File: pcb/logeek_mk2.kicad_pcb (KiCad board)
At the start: 2 copper layers, 68.6 x 53.3 mm, 138 parts, among them P1 Power, P10 XH2.54-2P RA, P11 BARREL_JACK, P12 USB_B, P13 DC3 5x2, P14 Power, P15 Analog, P16 Digital, P17 Digital, P2 Analog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

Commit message: Part value update.
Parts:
- C18: value 22uF -> 10uF
- D1, D2, D3, D7: value 1N5819 -> 1N5819WS
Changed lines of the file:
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@@
     (visible_elements 7FFDF121)
     (pcbplotparams
-      (layerselection 0x00020_00000000)
+      (layerselection 0x010fc_80000001)
       (usegerberextensions false)
       (excludeedgelayer false)
       (linewidth 0.100000)
-      (plotframeref false)
+      (plotframeref true)
       (viasonmask false)
       (mode 1)
@@
       (psa4output false)
       (plotreference true)
-      (plotvalue true)
-      (plotinvisibletext true)
+      (plotvalue false)
+      (plotinvisibletext false)
       (padsonsilk false)
       (subtractmaskfromsilk false)
       (outputformat 4)
       (mirror false)
-      (drillshape 0)
+      (drillshape 2)
       (scaleselection 1)
       (outputdirectory gerber/))
@@
       (effects (font (size 0.8 0.8) (thickness 0.15)))
     )
-    (fp_text value 1N5819 (at 0 0 270) (layer F.Fab)
+    (fp_text value 1N5819WS (at 0 0 270) (layer F.Fab)
       (effects (font (size 0.8 0.8) (thickness 0.15)))
     )
@@
       (effects (font (size 0.8 0.8) (thickness 0.15)))
     )
-    (fp_text value 22uF (at 0 0 270) (layer F.Fab)
+    (fp_text value 10uF (at 0 0 270) (layer F.Fab)
       (effects (font (size 0.8 0.8) (thickness 0.15)))
     )
@@
       (effects (font (size 0.8 0.8) (thickness 0.15)))
     )
-    (fp_text value 1N5819 (at 0 0 270) (layer F.Fab)
+    (fp_text value 1N5819WS (at 0 0 270) (layer F.Fab)
       (effects (font (size 0.8 0.8) (thickness 0.15)))
     )
@@
       (effects (font (size 0.8 0.8) (thickness 0.15)))
     )
-    (fp_text value 1N5819 (at -0.635 0) (layer F.Fab)
+    (fp_text value 1N5819WS (at -0.635 0) (layer F.Fab)
       (effects (font (size 0.8 0.8) (thickness 0.15)))
     )
@@
       (effects (font (size 1 1) (thickness 0.15)))
     )
-    (fp_text value 1N5819 (at -0.635 0) (layer F.Fab)
+    (fp_text value 1N5819WS (at -0.635 0) (layer F.Fab)
       (effects (font (size 0.8 0.8) (thickness 0.15)))
     )

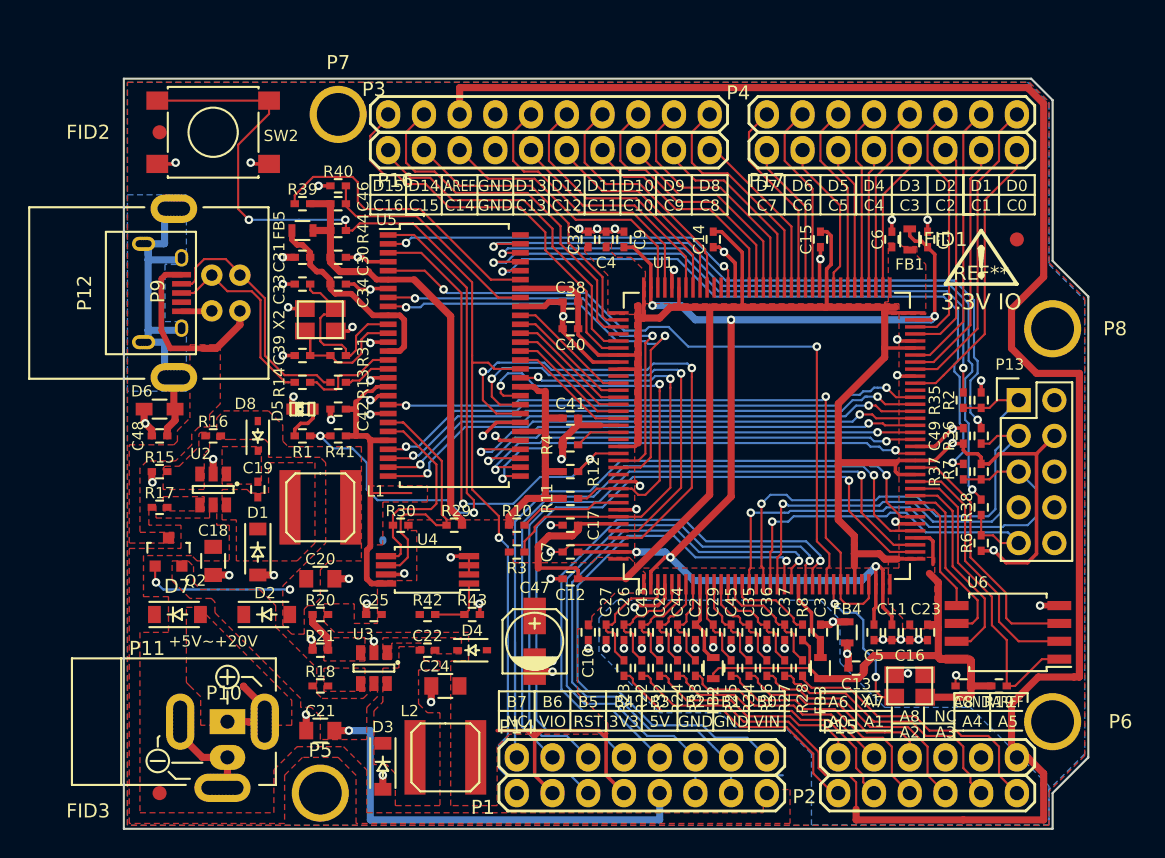
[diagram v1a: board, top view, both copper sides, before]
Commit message: Corrected FPGA footprint. Delete extra oscillator. Update silkscreen.
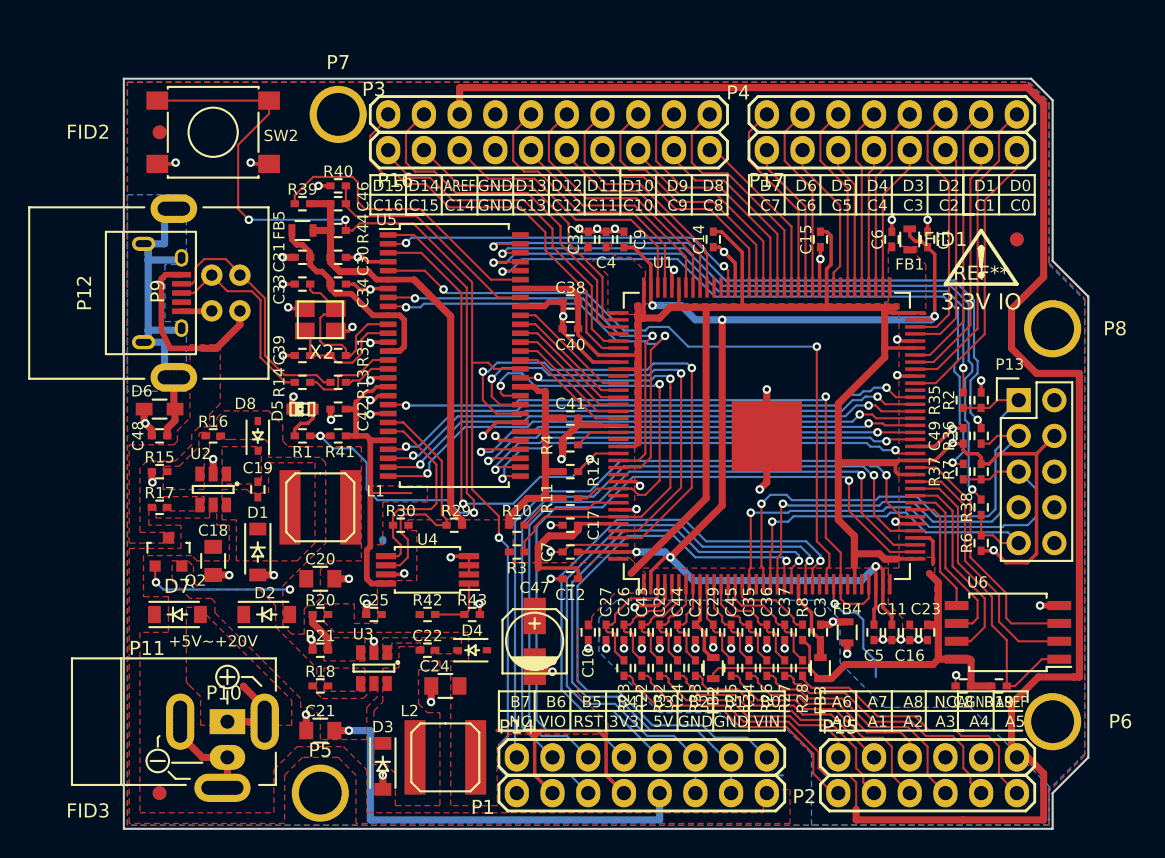
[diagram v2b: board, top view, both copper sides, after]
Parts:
- removed C13: 0.1uF, Capacitors_SMD:C_0402
- removed X1: 25MHz 50ppm, OSC3225
- C27, C28, C29, C35, C36, C37, C43, C44, C45: value 0.1uF -> 1nF
- R1, R41: value 220 -> 330
- U1: footprint Housings_QFP:TQFP-144_20x20mm_Pitch0.5mm -> Logeek_MK2:TQFP-144EP_20x20mm_Pitch0.5mm
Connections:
- U1 pad 28: /USERCLK -> Net-(U1-Pad28)
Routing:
- net +3V3: track 297.6 -> 286.0 mm
- net /USERCLK: track 10.9 -> 0.00 mm, vias 2 -> 0
- net Net-(U1-Pad28): track 0.00 -> 8.36 mm, vias 0 -> 1
- net GNDD: track 126.9 -> 132.2 mm, vias 63 -> 64

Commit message: Updated socket footprints.
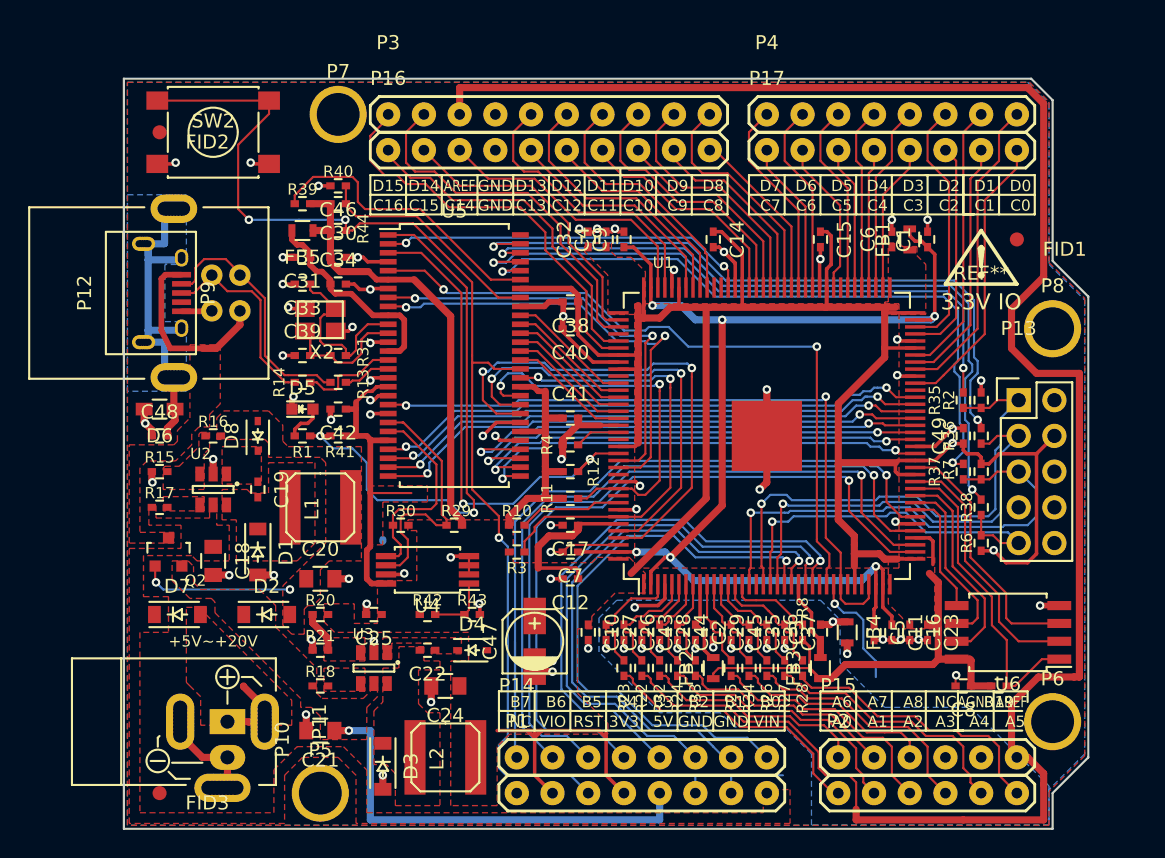
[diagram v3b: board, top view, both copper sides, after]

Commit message: Footprints update.
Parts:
- C47: footprint Capacitors_SMD:c_elec_4x5.8 -> Logeek_MK2:TantalC_SizeB_EIA-3528_HandSoldering
- D5: value LED GREEN -> LED TRUE GREEN; footprint LEDs:LED-0603 -> Logeek_MK2:LED-0603
- D6: footprint Resistors_SMD:R_0603_HandSoldering -> Logeek_MK2:R_0402_HandSoldering
- R41: value 330 -> 1K
- X2: footprint Crystals_Oscillators_SMD:crystal_FA238-TSX3225 -> Logeek_MK2:XTAL3225
- moved C47 0.64 mm to (140.2, 112.4)
- moved C8 0.13 mm to (170.7, 116.1)
- moved R19 0.13 mm to (173.2, 116.1)
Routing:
- net Net-(U1-Pad28): track 8.36 -> 0.00 mm, vias 1 -> 0
- net GNDD: track 132.2 -> 135.0 mm
- net +3V3: track 286.0 -> 287.7 mm, vias 2 -> 4

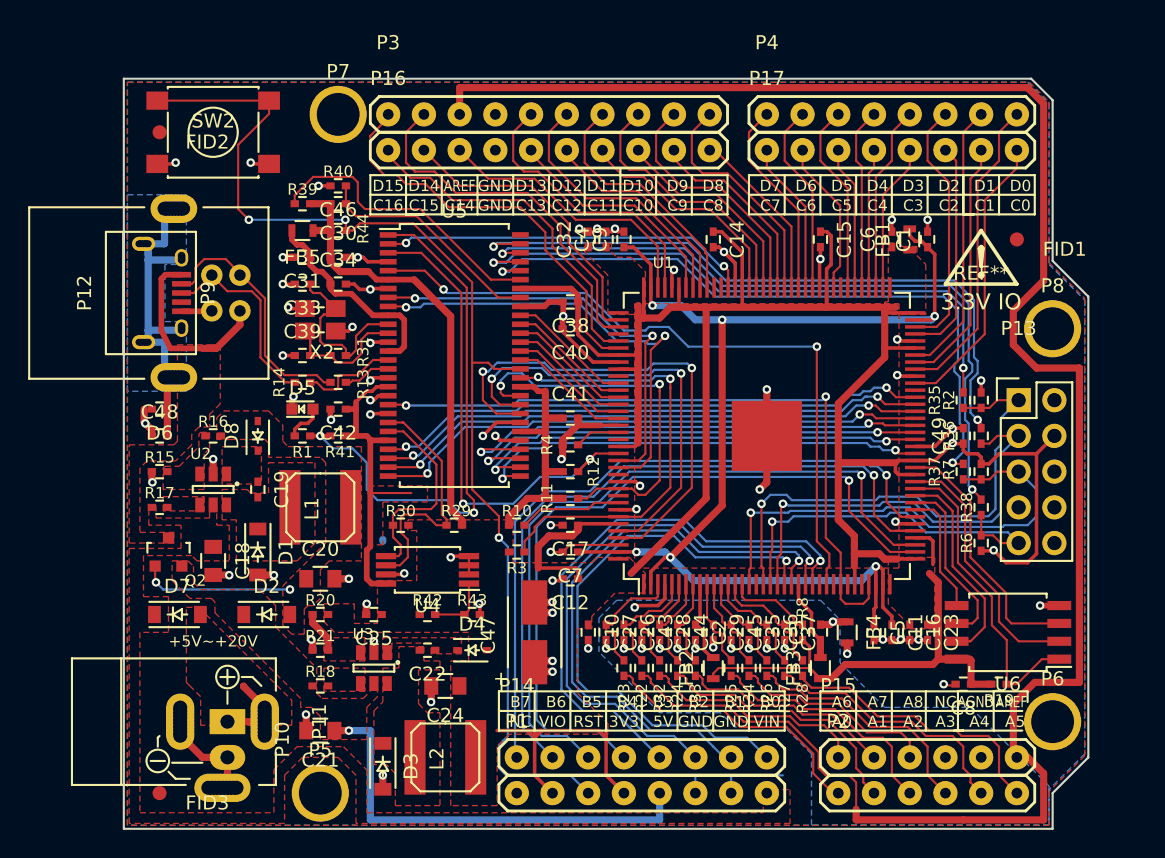
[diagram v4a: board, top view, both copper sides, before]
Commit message: Add EXTCLK.
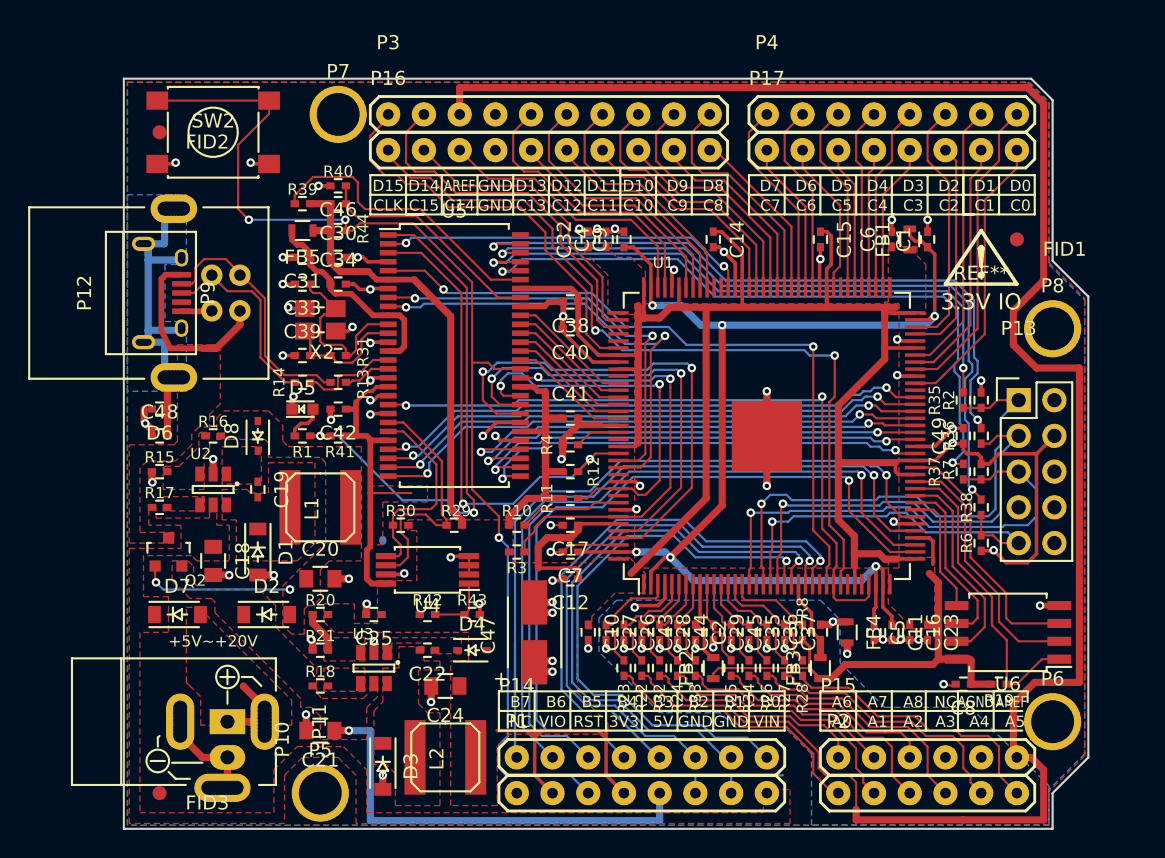
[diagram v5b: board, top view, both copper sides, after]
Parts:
- R41: value 1K -> 1k
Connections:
- P16 pad 1: /C16 -> /EXTCLK
- U1 pad 113: /C16 -> Net-(U1-Pad113)
- U1 pad 28: Net-(U1-Pad28) -> /IFCLK
- U1 pad 29: /IFCLK -> /EXTCLK
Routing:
- net /EXTCLK: track 0.00 -> 57.4 mm, vias 0 -> 2
- net /C16: track 24.7 -> 0.00 mm
- net /LEDEN: track 39.8 -> 38.7 mm
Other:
- board text added: "CLK"
- board text removed: "C16"

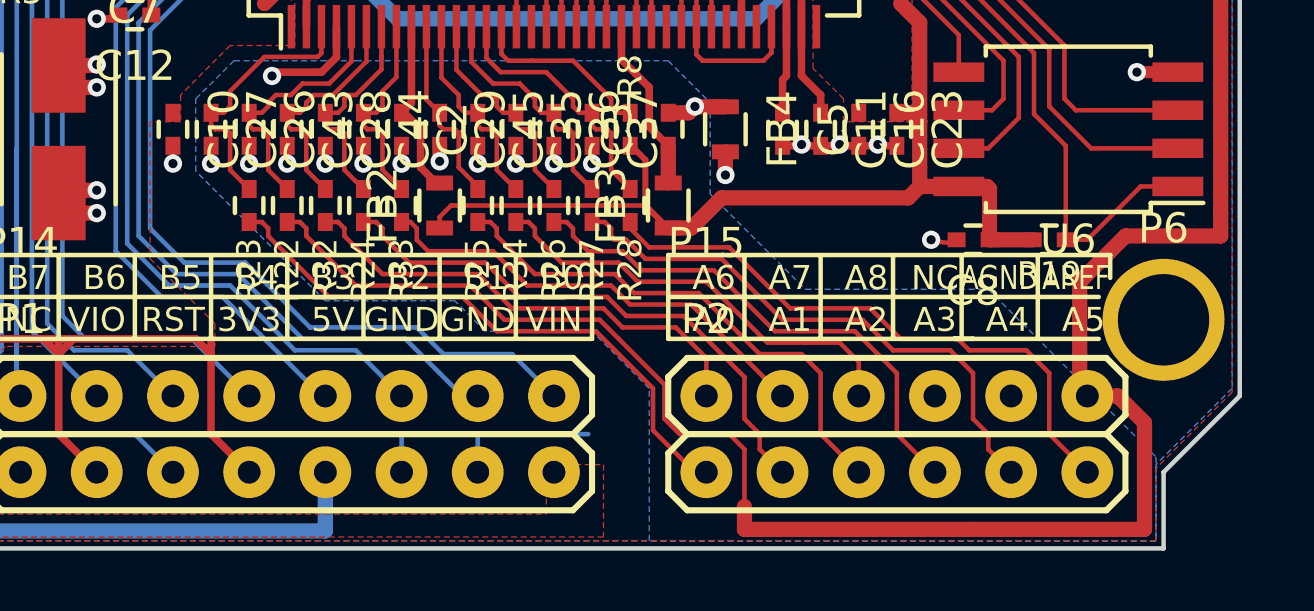
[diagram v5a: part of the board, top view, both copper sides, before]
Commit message: Analog pin-mapping changed to support VIN monitoring.
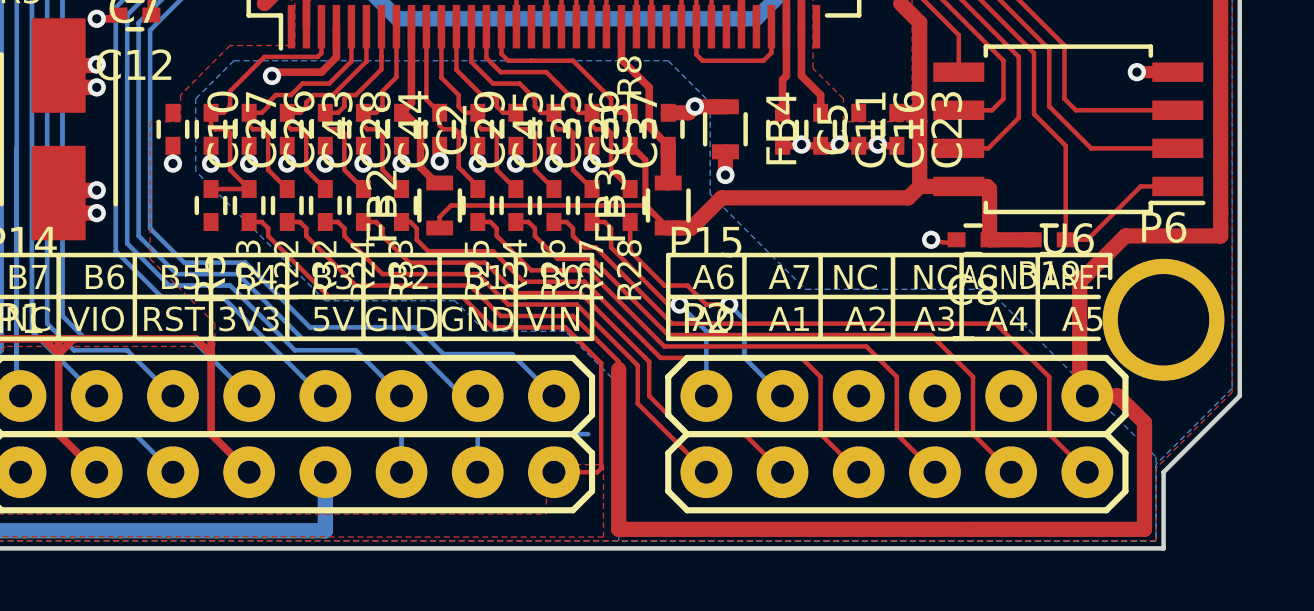
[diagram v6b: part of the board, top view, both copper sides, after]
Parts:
- added R5: 1k, Logeek_MK2:R_0402_HandSoldering, F.Cu at (145.3, 114.9)
- R23: value 22 -> 10k
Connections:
- C27 pad 1: /AIN0 -> /VMON
- C29 pad 1: /AIN2 -> /AIN3
- C35 pad 1: /AIN3 -> /AIN5
- C36 pad 1: /AIN4 -> /AIN6
- C37 pad 1: /AIN5 -> /AIN7
- C43 pad 1: /AIN6 -> /AIN0
- C44 pad 1: /AIN7 -> /AIN2
- C45 pad 1: /AIN8 -> /AIN4
- R23 pad 1: /AIN0 -> /VMON
- R23 pad 2: /A0 -> /VIN_SAFE
- R25 pad 1: /AIN2 -> /AIN3
- R25 pad 2: /A2 -> /A3
- R26 pad 1: /AIN3 -> /AIN5
- R26 pad 2: /A3 -> /A5
- R27 pad 1: /AIN4 -> /AIN6
- R27 pad 2: /A4 -> /A6
- R28 pad 1: /AIN5 -> /AIN7
- R28 pad 2: /A5 -> /A7
- R32 pad 1: /AIN6 -> /AIN0
- R32 pad 2: /A6 -> /A0
- R33 pad 1: /AIN7 -> /AIN2
- R33 pad 2: /A7 -> /A2
- R34 pad 1: /AIN8 -> /AIN4
- R34 pad 2: /A8 -> /A4
- U1 pad 10: /AIN2 -> /AIN3
- U1 pad 11: /AIN8 -> /AIN4
- U1 pad 12: /AIN3 -> /AIN5
- U1 pad 13: /AIN4 -> /AIN6
- U1 pad 14: /AIN5 -> /AIN7
- U1 pad 3: /AIN0 -> /VMON
- U1 pad 6: /AIN6 -> /AIN0
- U1 pad 8: /AIN7 -> /AIN2
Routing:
- net /VIN_SAFE: track 0.00 -> 19.0 mm
- net /A8: track 14.7 -> 0.00 mm
- net /VMON: track 0.00 -> 10.3 mm
- net /A6: track 16.0 -> 7.85 mm, vias 0 -> 1
- net /AIN8: track 6.95 -> 0.00 mm
- net /A7: track 15.2 -> 9.52 mm, vias 0 -> 1
- net /A0: track 19.7 -> 17.0 mm
- net /A2: track 17.5 -> 20.0 mm
- net /A5: track 20.0 -> 22.5 mm
- net /A3: track 17.5 -> 20.0 mm
- net /A4: track 18.8 -> 21.2 mm
- net /AIN7: track 6.95 -> 8.76 mm
- net /AIN5: track 8.76 -> 7.45 mm
- net /AIN4: track 8.07 -> 6.95 mm
- net /AIN3: track 7.45 -> 6.34 mm
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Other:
- board text removed: "A8"
